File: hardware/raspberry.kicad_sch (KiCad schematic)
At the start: 19 parts, among them J3 Conn_01x04, U1 RP2040, U2 W25Q128JVS, Y1 Crystal_GND24

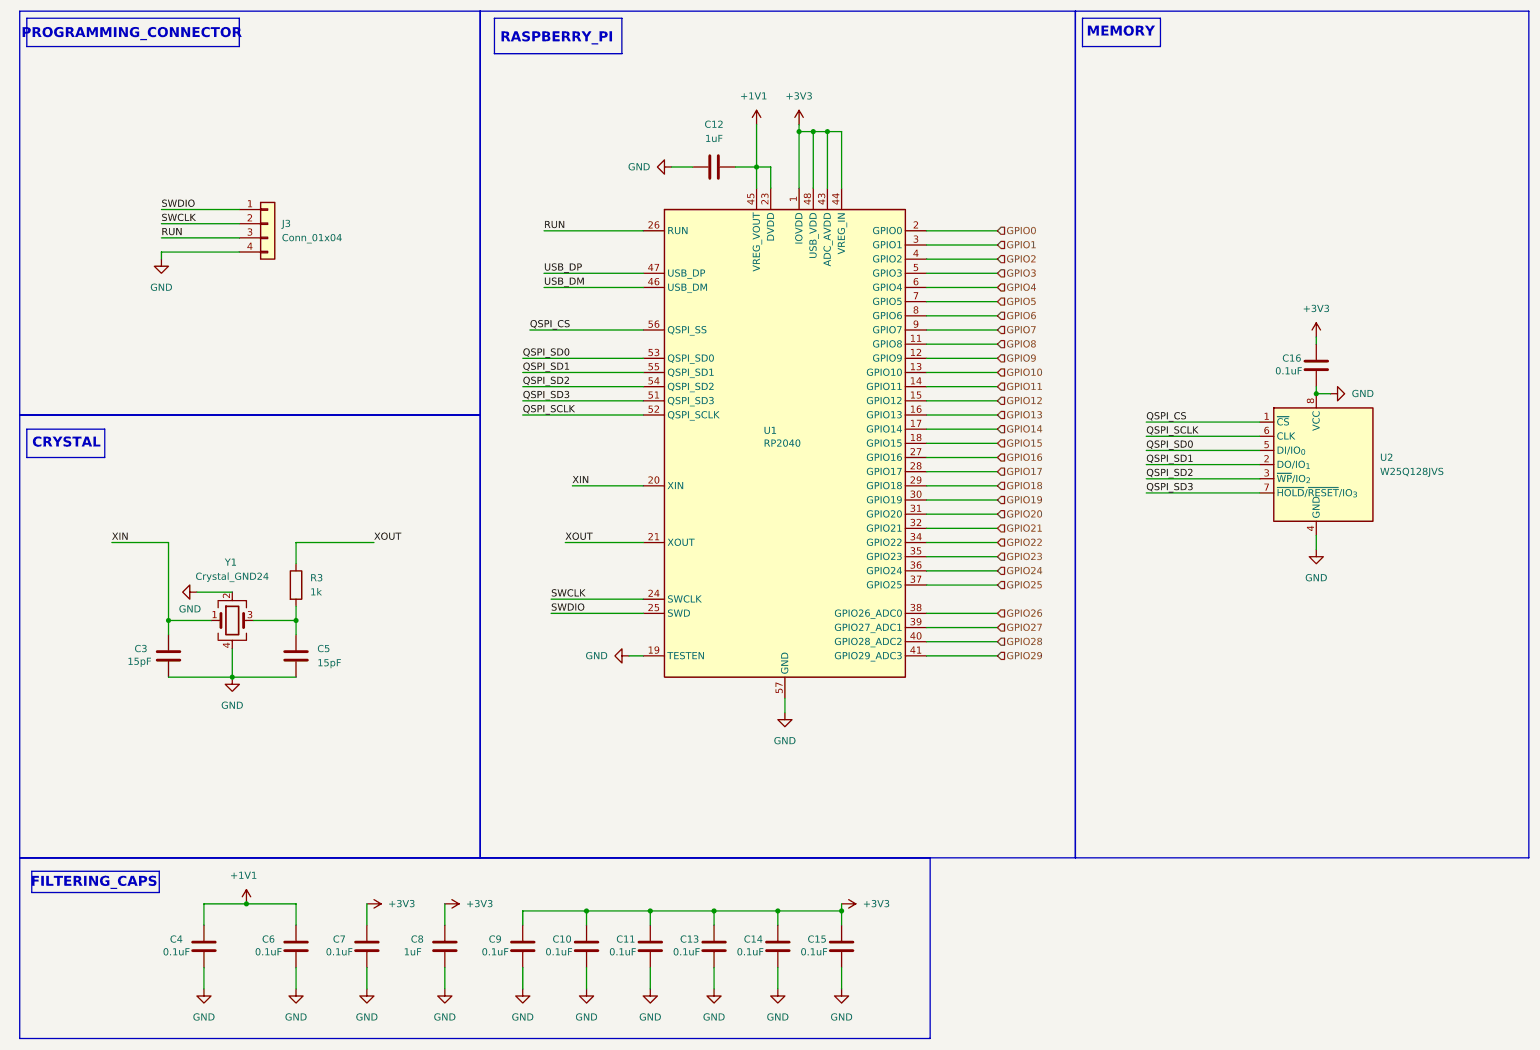
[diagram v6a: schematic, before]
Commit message: test points added to the schematic
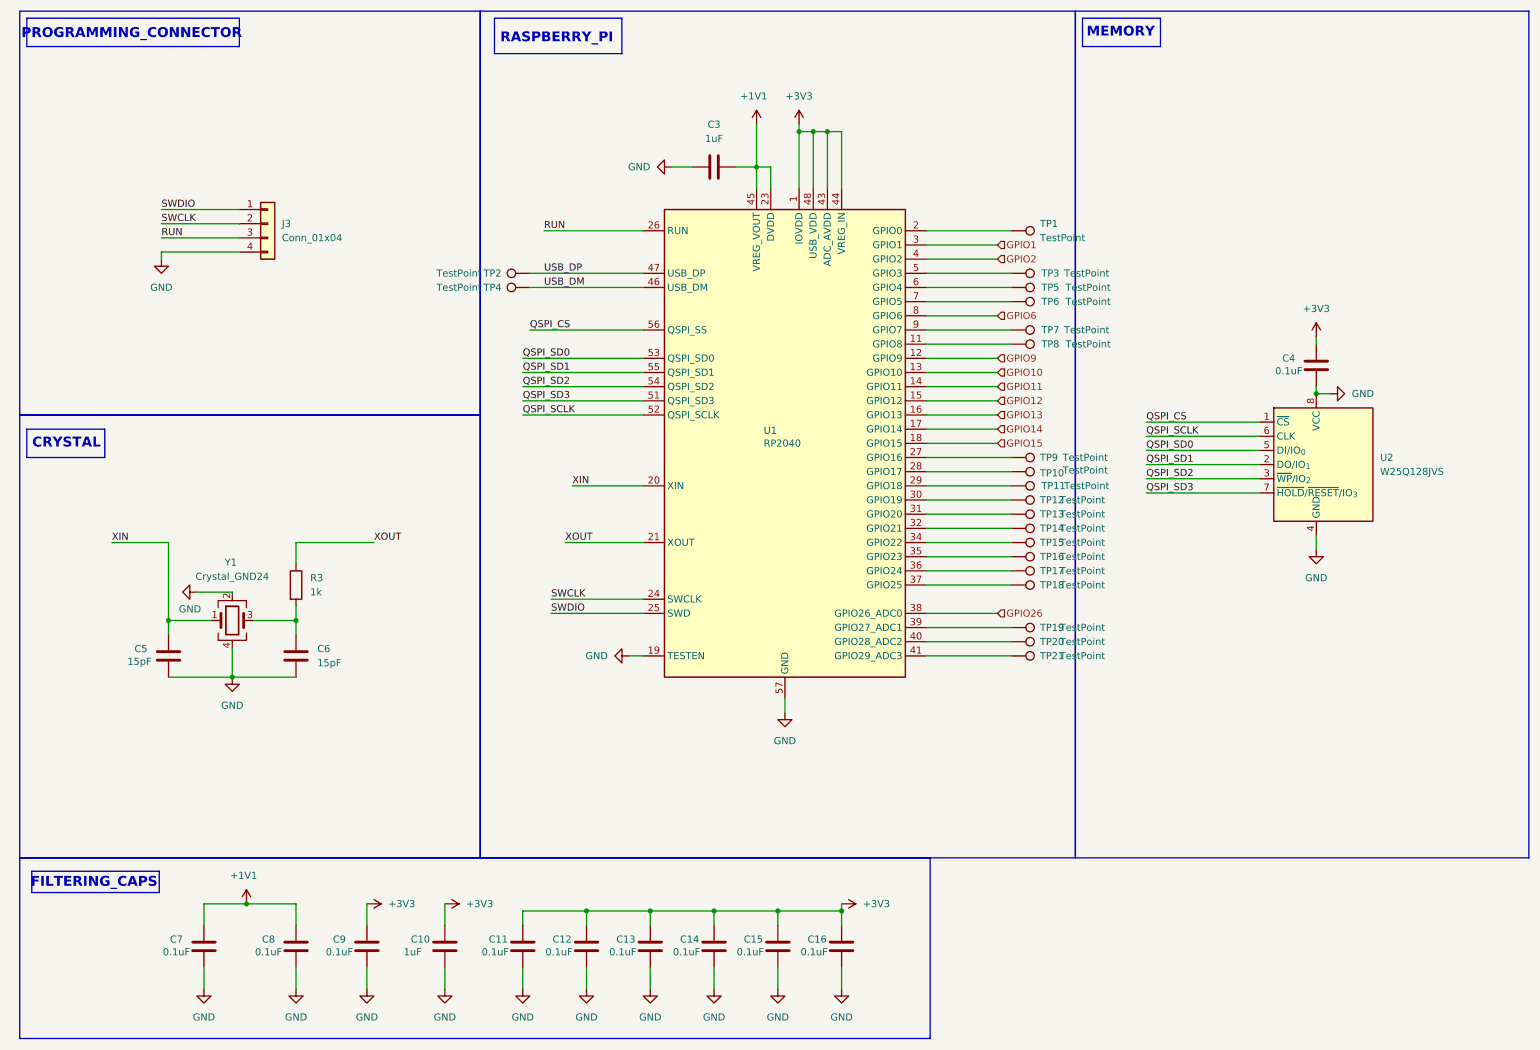
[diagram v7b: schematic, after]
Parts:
- added TP1, TP10, TP11, TP12, TP13, TP14, TP15, TP16, TP17, TP18, TP19, TP2, TP20, TP21, TP3, TP4, TP5, TP6, TP7, TP8, TP9: TestPoint, TestPoint:TestPoint_Pad_D1.5mm, symbol Connector:TestPoint
- renumbered C8 to C10, C9 to C11, C10 to C12, C11 to C13, C13 to C14, C14 to C15, C15 to C16, C12 to C3, C16 to C4, C3 to C5, C5 to C6, C4 to C7, C6 to C8, C7 to C9
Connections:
- net USB_DM: now also TP4.1
- net USB_DP: now also TP2.1
- net GPIO0: no longer names the net of U1.2 (GPIO0)
- net GPIO0: now also TP1.1
- net GPIO16: no longer names the net of U1.27 (GPIO16)
- net GPIO16: now also TP9.1
- net GPIO17: no longer names the net of U1.28 (GPIO17)
- net GPIO17: now also TP10.1
- net GPIO18: no longer names the net of U1.29 (GPIO18)
- net GPIO18: now also TP11.1
- net GPIO19: no longer names the net of U1.30 (GPIO19)
- net GPIO19: now also TP12.1
- net GPIO20: no longer names the net of U1.31 (GPIO20)
- net GPIO20: now also TP13.1
- net GPIO21: no longer names the net of U1.32 (GPIO21)
- net GPIO21: now also TP14.1
- net GPIO22: no longer names the net of U1.34 (GPIO22)
- net GPIO22: now also TP15.1
- net GPIO23: no longer names the net of U1.35 (GPIO23)
- net GPIO23: now also TP16.1
- net GPIO24: no longer names the net of U1.36 (GPIO24)
- net GPIO24: now also TP17.1
- net GPIO25: no longer names the net of U1.37 (GPIO25)
- net GPIO25: now also TP18.1
- net GPIO27: no longer names the net of U1.39 (GPIO27_ADC1)
- net GPIO27: now also TP19.1
- net GPIO28: no longer names the net of U1.40 (GPIO28_ADC2)
- net GPIO28: now also TP20.1
- net GPIO29: no longer names the net of U1.41 (GPIO29_ADC3)
- net GPIO29: now also TP21.1
- net GPIO3: no longer names the net of U1.5 (GPIO3)
- net GPIO3: now also TP3.1
- net GPIO4: no longer names the net of U1.6 (GPIO4)
- net GPIO4: now also TP5.1
- net GPIO5: no longer names the net of U1.7 (GPIO5)
- net GPIO5: now also TP6.1
- net GPIO7: no longer names the net of U1.9 (GPIO7)
- net GPIO7: now also TP7.1
- net GPIO8: no longer names the net of U1.11 (GPIO8)
- net GPIO8: now also TP8.1

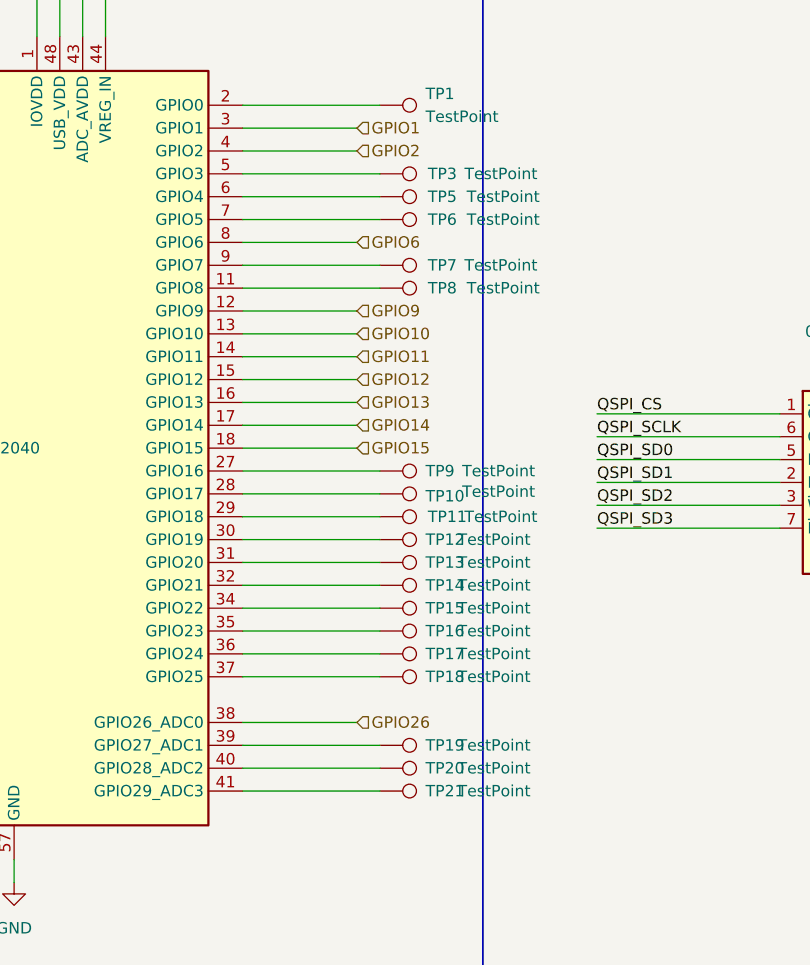
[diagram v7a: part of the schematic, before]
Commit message: test points placed on the pcb
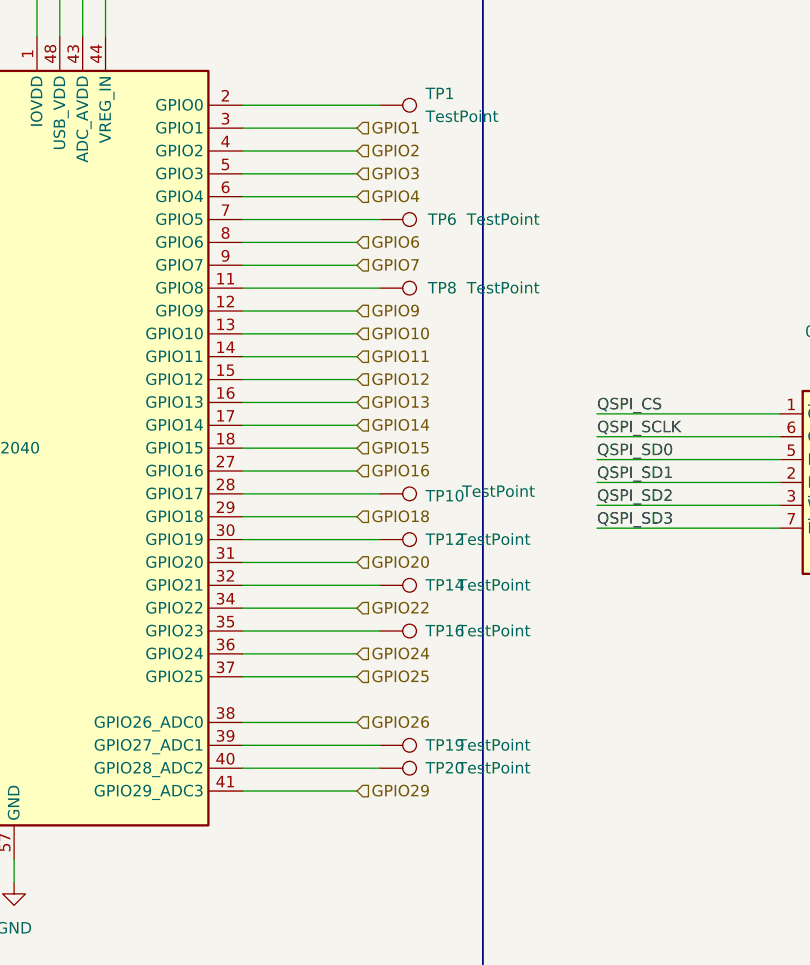
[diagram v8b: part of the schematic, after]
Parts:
- removed TP11, TP13, TP15, TP17, TP18, TP21, TP3, TP5, TP7, TP9: TestPoint, TestPoint:TestPoint_Pad_D1.5mm, symbol Connector:TestPoint
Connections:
- net GPIO3: now reaches U1.5 (GPIO3)
- net GPIO4: now reaches U1.6 (GPIO4)
- net GPIO29: now reaches U1.41 (GPIO29_ADC3)
- net GPIO18: now reaches U1.29 (GPIO18)
- net GPIO24: now reaches U1.36 (GPIO24)
- net GPIO16: now reaches U1.27 (GPIO16)
- net GPIO20: now reaches U1.31 (GPIO20)
- net GPIO22: now reaches U1.34 (GPIO22)
- net GPIO25: now reaches U1.37 (GPIO25)
- net GPIO7: now reaches U1.9 (GPIO7)
